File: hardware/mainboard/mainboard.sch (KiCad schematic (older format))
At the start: 12 parts, among them J1 Conn_01x03, J2 Conn_01x03, J3 Conn_01x03, J4 Conn_01x03, J5 Conn_01x03, SW1 Rotary_Encoder_Switch

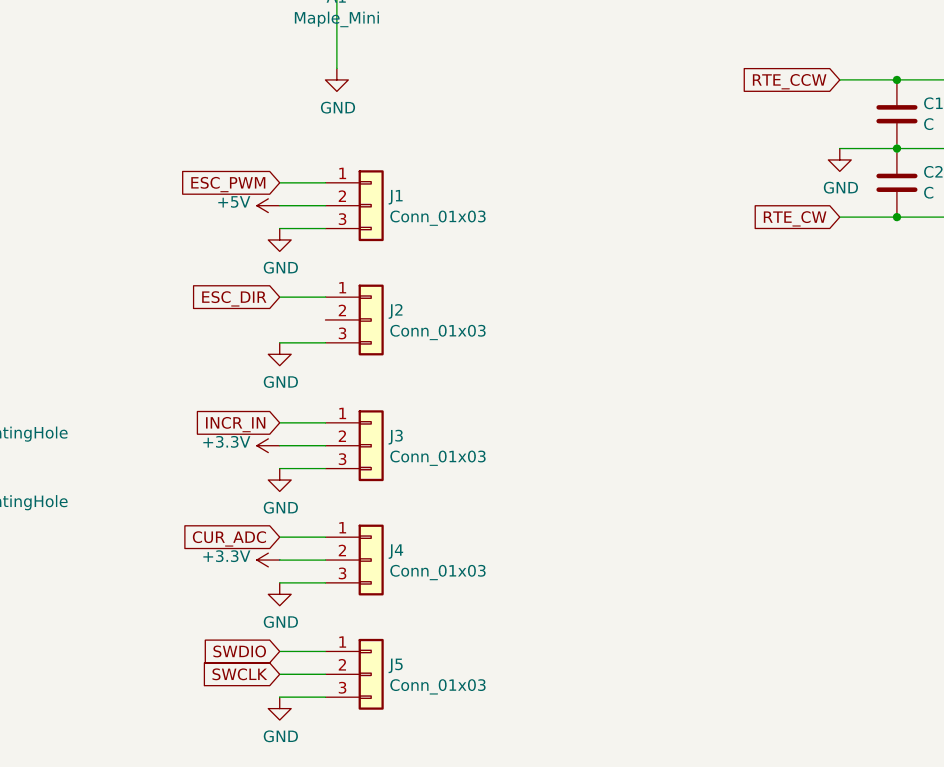
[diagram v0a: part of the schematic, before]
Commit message: generated gerber files for jlcpcb
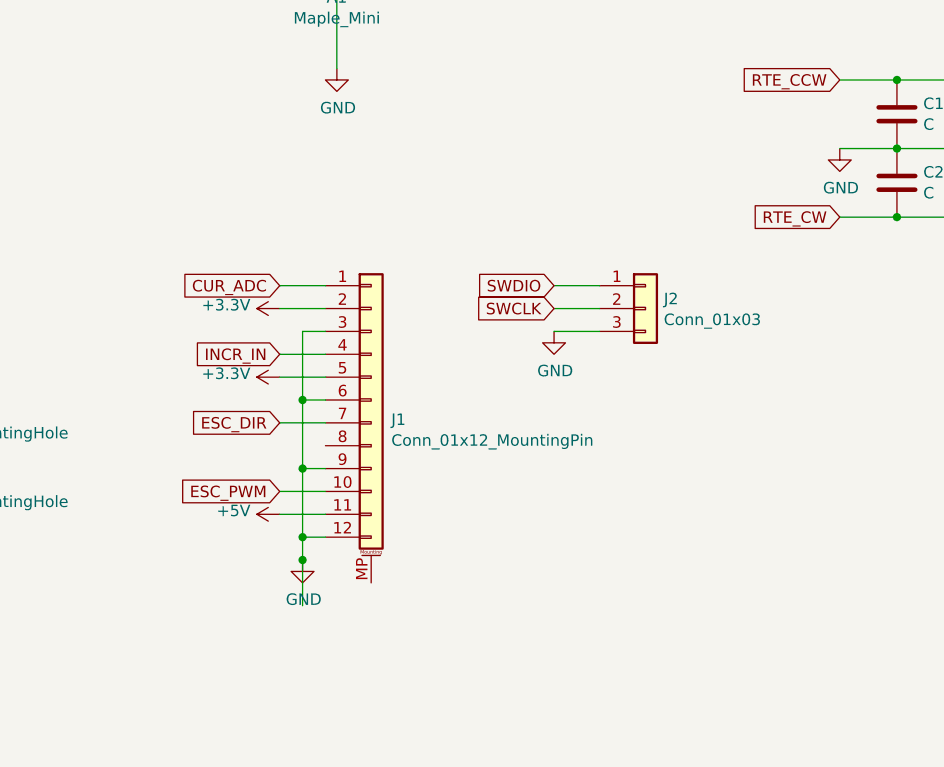
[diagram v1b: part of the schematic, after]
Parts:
- removed J1, J2, J3, J4: Conn_01x03, Connector_PinHeader_2.54mm:PinHeader_1x03_P2.54mm_Horizontal, symbol Connector_Generic:Conn_01x03
- added J1: Conn_01x12_MountingPin, Connector_PinHeader_2.54mm:PinHeader_1x12_P2.54mm_Horizontal, symbol Connector_Generic_MountingPin:Conn_01x12_MountingPin
- renumbered J5 to J2
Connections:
- net +3V3: now also J1.2 (Pin_2), J1.5 (Pin_5)
- net +5V: now also J1.11 (Pin_11)
- net CUR_ADC: now also J1.1 (Pin_1)
- net ESC_DIR: now also J1.7 (Pin_7)
- net ESC_PWM: now also J1.10 (Pin_10)
- net GND: now also J1.12 (Pin_12), J1.3 (Pin_3), J1.6 (Pin_6), J1.9 (Pin_9)
- net INCR_IN: now also J1.4 (Pin_4)
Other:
- moved on the sheet: J2
